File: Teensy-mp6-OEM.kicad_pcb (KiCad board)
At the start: 2 copper layers, 64.8 x 24.8 mm, 4 parts, among them J1 CONN_01X03, U1 Teensy_3.2, U2 mp6-OEM, U3 mp6-pump-conector

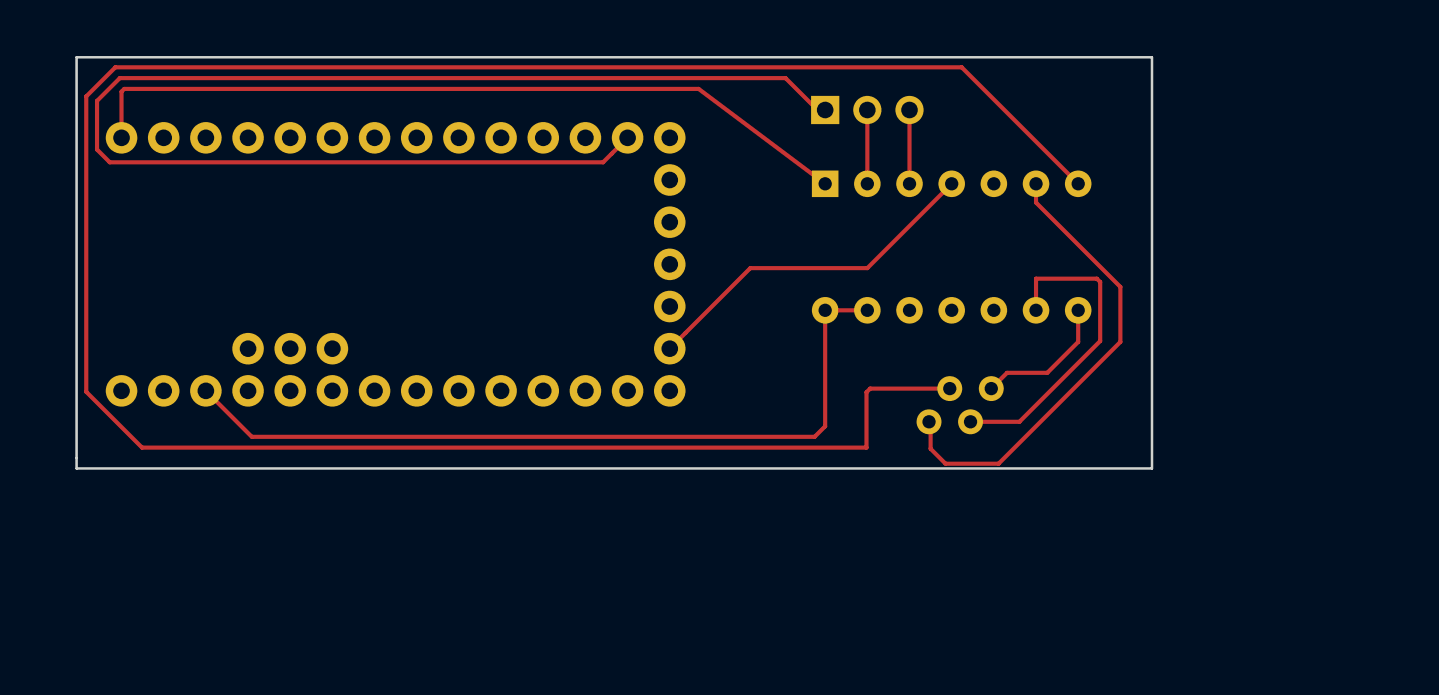
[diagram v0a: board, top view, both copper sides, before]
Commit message: Increase HV track widths, Change Teensy 3.3V and GND pins, Move Molex Connector
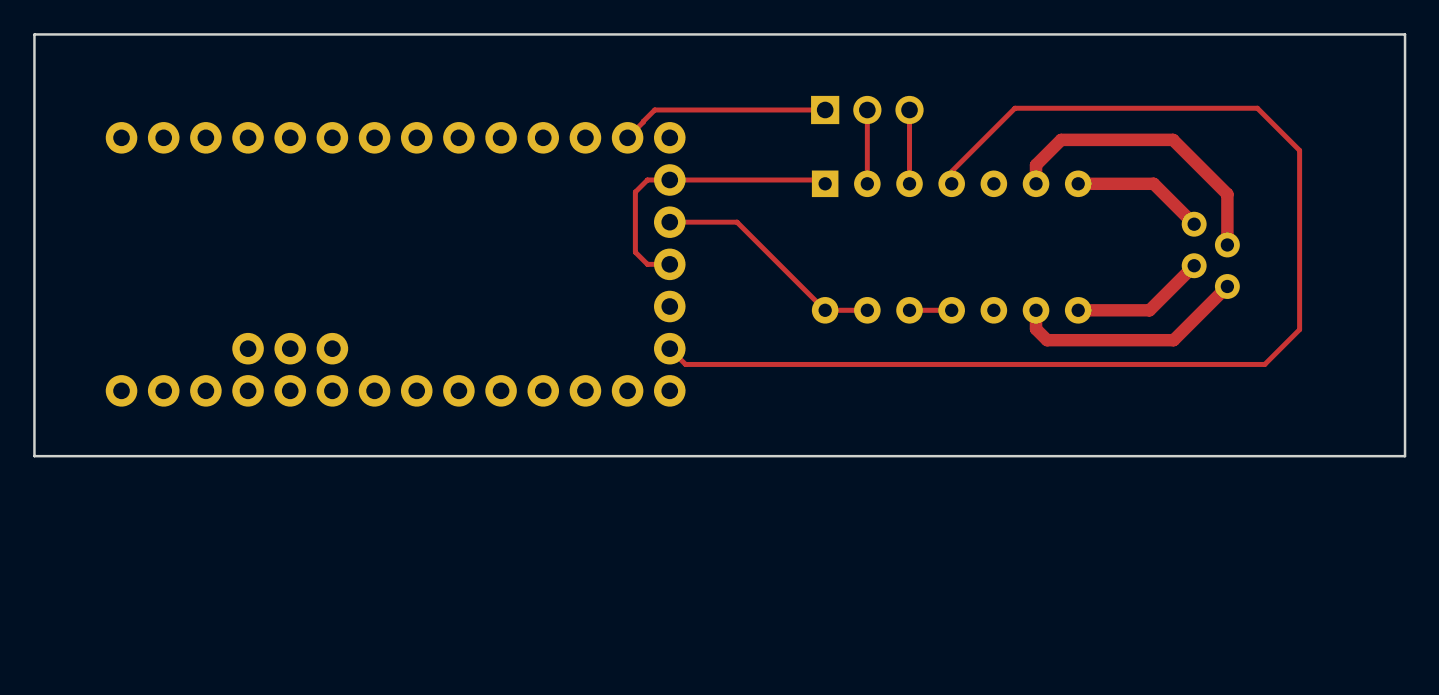
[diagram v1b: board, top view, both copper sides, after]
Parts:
- moved U3 17.5 mm to (197.8, 108.4), turned to 0 degrees
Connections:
- U1 pad 24: +3V3 -> Net-(U1-Pad24)
- U1 pad 27: GND -> Net-(U1-Pad27)
- U1 pad 30: Net-(U1-Pad30) -> GND
- U1 pad 31: Net-(U1-Pad31) -> +3V3
- U1 pad 32: Net-(U1-Pad32) -> GND
- U2 pad 12: Net-(U2-Pad12) -> Net-(U2-Pad11)
- U3 pad 1: Net-(U2-Pad6) -> Net-(U2-Pad9)
- U3 pad 2: Net-(U2-Pad7) -> Net-(U2-Pad8)
- U3 pad 3: Net-(U2-Pad9) -> Net-(U2-Pad6)
- U3 pad 4: Net-(U2-Pad8) -> Net-(U2-Pad7)
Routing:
- net Net-(U2-Pad7): track 138.0 -> 7.99 mm
- net Net-(J1-Pad1): track 81.7 -> 12.6 mm
- net Net-(U1-Pad28): track 21.1 -> 74.3 mm
- net +3V3: track 48.2 -> 14.1 mm
- net GND: track 47.1 -> 17.5 mm
- net Net-(U2-Pad6): track 28.1 -> 17.7 mm
- net Net-(U2-Pad9): track 19.2 -> 14.3 mm
- net Net-(U2-Pad11): track 0.00 -> 2.54 mm
- net Net-(J1-Pad2): track 4.71 -> 3.81 mm
- net Net-(J1-Pad3): track 4.71 -> 3.81 mm
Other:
- board size 64.8 x 24.8 mm -> 82.6 x 25.4 mm
- net class Default: trace_width 0.25 -> 0.3
- net class Large added: clearance 0.4, trace_width 0.45, via_dia 0.6, via_drill 0.4
- rule trace_min: 0.2 -> 0.3

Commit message: Added connector from PMT Control Board
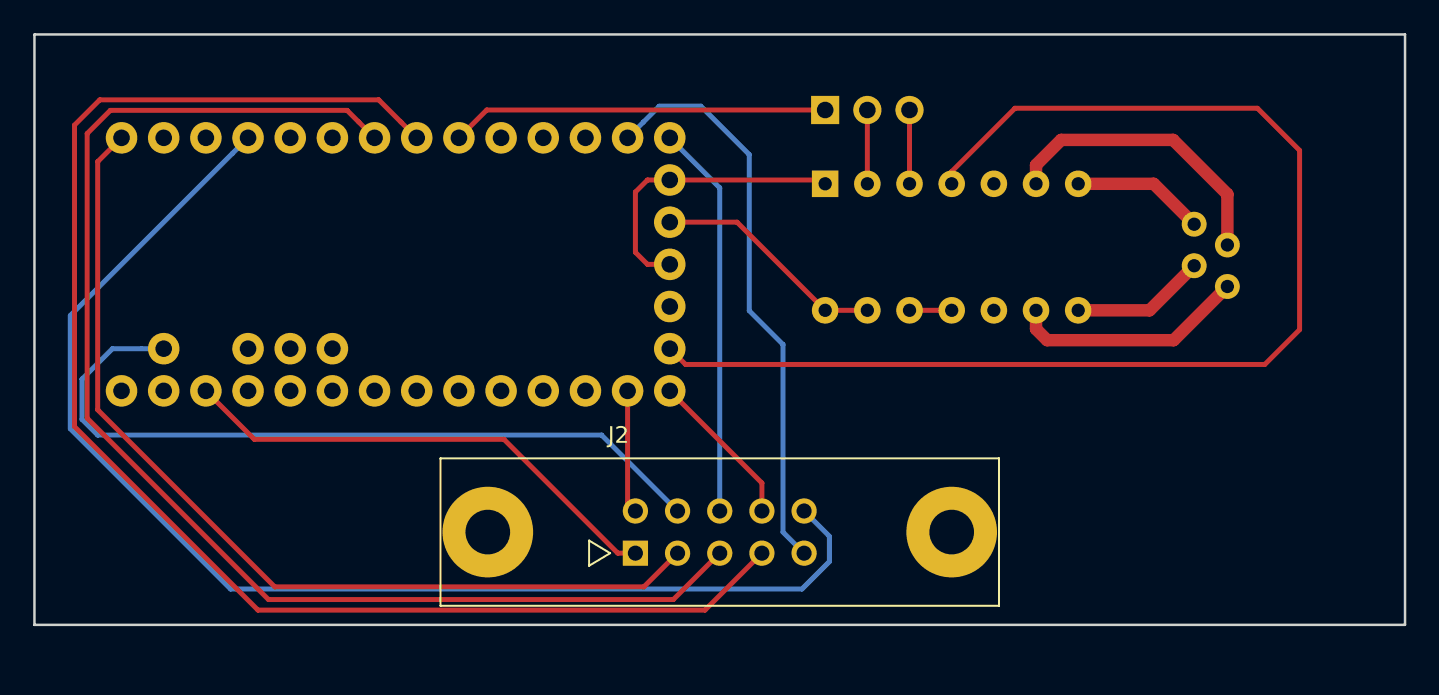
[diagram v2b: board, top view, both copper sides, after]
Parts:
- added J2: CONN_02X05, Connectors:he10-10d, F.Cu at (163.2, 126.5)
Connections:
- J1 pad 1: Net-(J1-Pad1) -> FREQ_PIN
- U1 pad 11: Net-(J1-Pad1) -> DOUT
- U1 pad 12: Net-(U1-Pad12) -> DIN
- U1 pad 13: Net-(U1-Pad13) -> SCK
- U1 pad 14: Net-(U1-Pad14) -> MONITOR
- U1 pad 2: Net-(U1-Pad2) -> SHUTTER
- U1 pad 24: Net-(U1-Pad24) -> +3.3V
- U1 pad 27: Net-(U1-Pad27) -> GND
- U1 pad 5: Net-(U1-Pad5) -> CS_POT
- U1 pad 6: Net-(U1-Pad6) -> CS_ADC
- U1 pad 7: Net-(U1-Pad7) -> FREQ_PIN
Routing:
- net CS_ADC: track 0.00 -> 88.0 mm
- net CS_POT: track 0.00 -> 79.5 mm
- net SHUTTER: track 0.00 -> 76.0 mm
- net GND: track 17.5 -> 74.7 mm
- net +5V(VUSB): track 0.00 -> 46.3 mm
- net DOUT: track 0.00 -> 34.7 mm
- net +3.3V: track 0.00 -> 29.9 mm
- net DIN: track 0.00 -> 23.7 mm, vias 0 -> 1
- net FREQ_PIN: track 0.00 -> 22.8 mm
- net Net-(J1-Pad1): track 12.6 -> 0.00 mm
- net SCK: track 0.00 -> 9.53 mm
- net MONITOR: track 0.00 -> 7.43 mm
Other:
- board size 82.6 x 25.4 mm -> 82.6 x 35.6 mm
- net class Default: clearance 0.4 -> 0.15
- net class Large: clearance 0.4 -> 0.15
- rule trace_clearance: 0.4 -> 0.15

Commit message: Rewire with different power
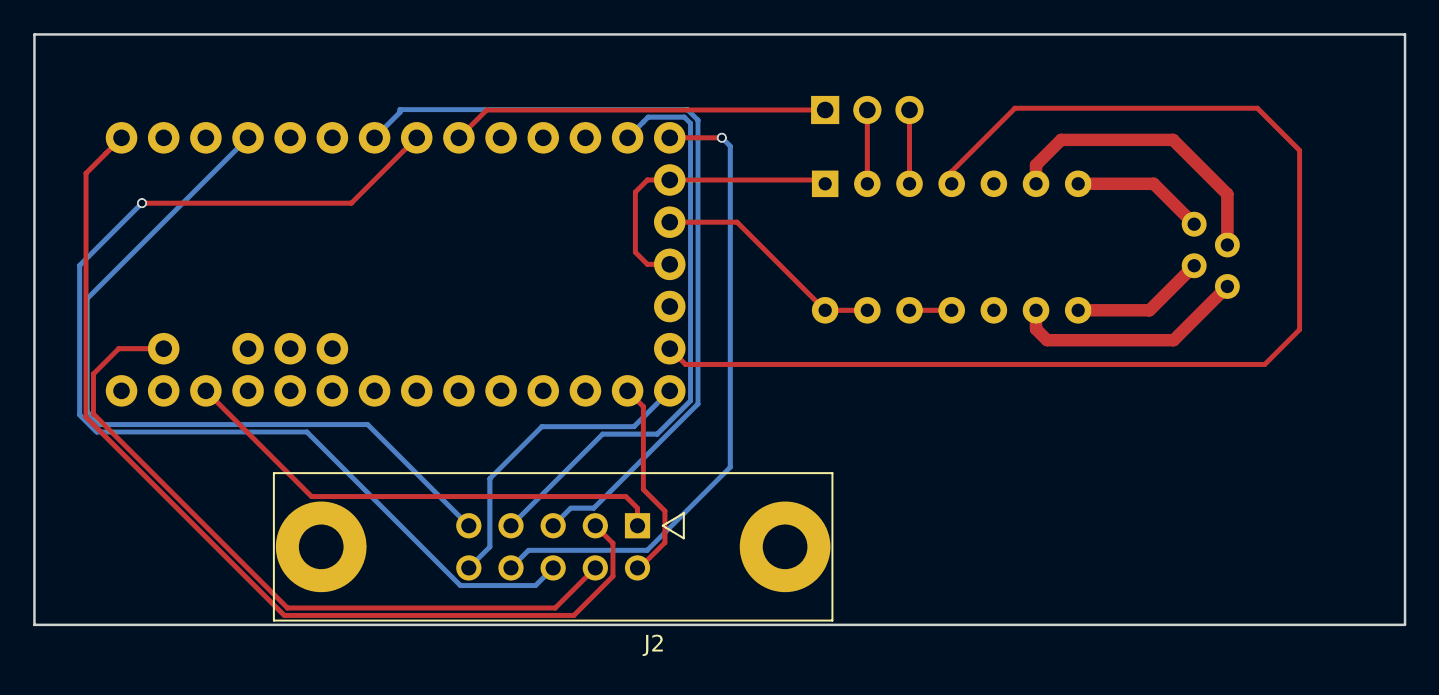
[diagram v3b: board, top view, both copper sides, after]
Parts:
- moved J2 1.66 mm to (163.3, 124.8), turned to 180 degrees
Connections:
- J2 pad 10: SHUTTER -> SCK
- J2 pad 6: DIN -> CS_ADC
- J2 pad 7: CS_ADC -> DOUT
- J2 pad 8: SCK -> DIN
- J2 pad 9: DOUT -> SHUTTER
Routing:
- net CS_POT: track 79.5 -> 49.4 mm
- net SHUTTER: track 76.0 -> 46.3 mm
- net CS_ADC: track 88.0 -> 65.7 mm, vias 0 -> 1
- net DIN: track 23.7 -> 38.9 mm
- net SCK: track 9.53 -> 18.9 mm, vias 0 -> 1
- net MONITOR: track 7.43 -> 12.4 mm
- net +5V(VUSB): track 46.3 -> 43.3 mm
- net GND: track 74.7 -> 76.4 mm
- net DOUT: track 34.7 -> 35.1 mm, vias 0 -> 1
